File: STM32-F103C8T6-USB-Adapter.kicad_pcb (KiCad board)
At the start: 2 copper layers, 86 x 39 mm, 64 parts, among them J1 USB_B_Micro, J2 Conn_01x06_Male, J3 Conn_01x04_Male, J4 Conn_01x06_Male, J5 Conn_01x05_Male, J6 Conn_01x04_Male, J7 Conn_01x04_Male, Q1 BC817, SW1 SW_Push, U1 SN65220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

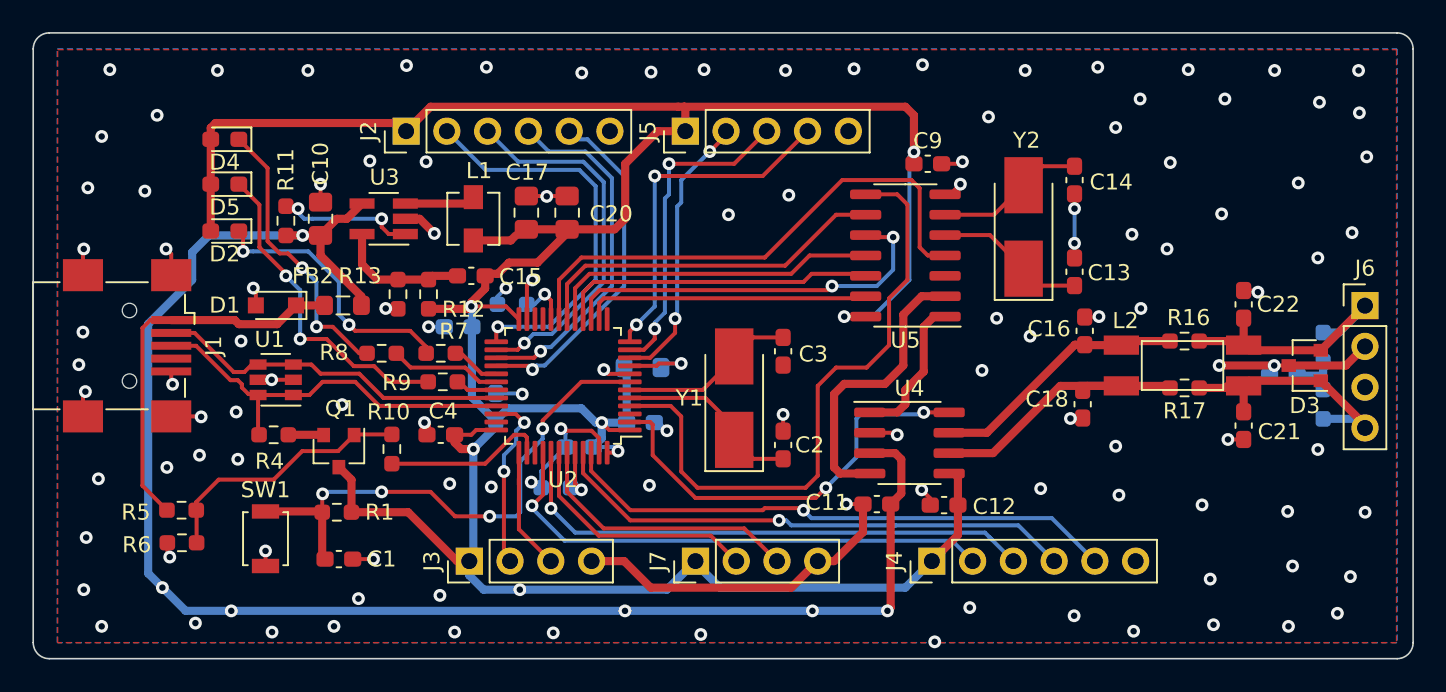
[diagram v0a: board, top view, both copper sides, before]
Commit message: optimize via of gnd copper
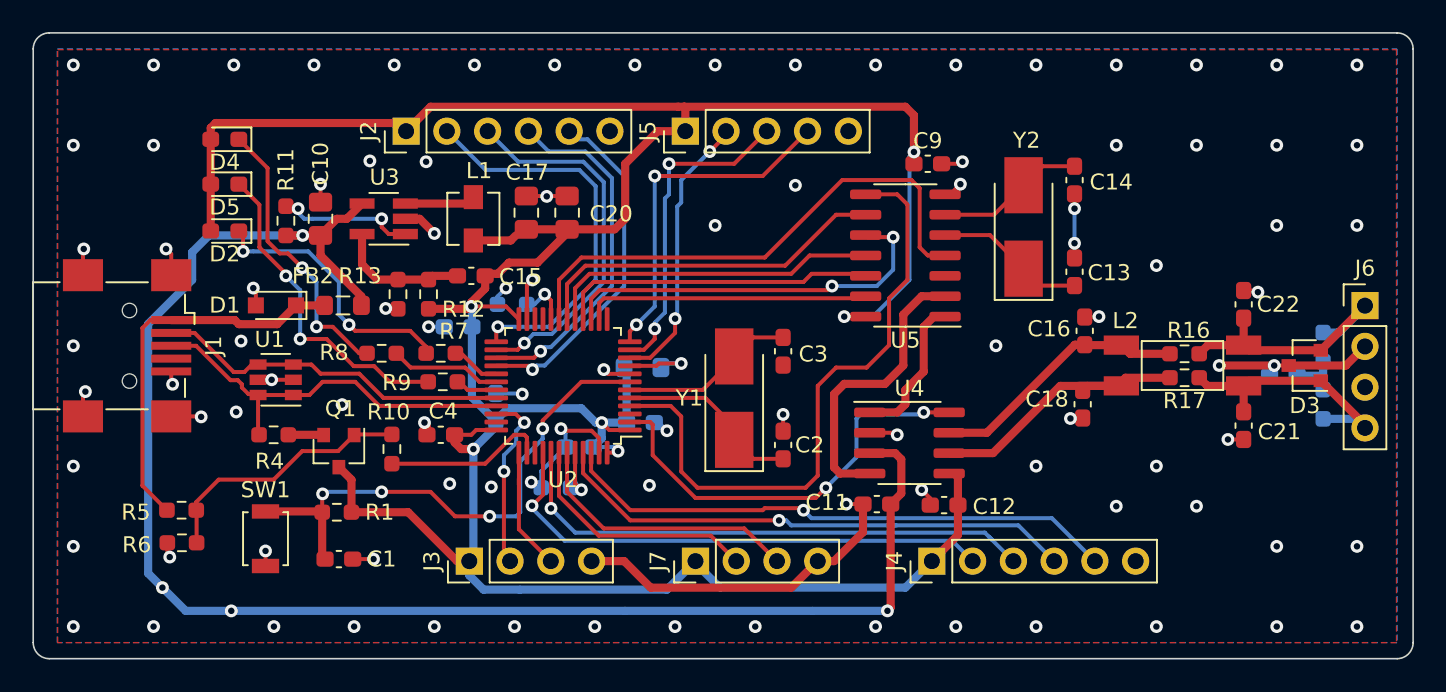
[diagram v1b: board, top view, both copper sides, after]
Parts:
- moved R16 0.79 mm to (171.8, 75.0)
- moved R17 0.63 mm to (171.8, 76.5)
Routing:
- net /CANL: track 18.3 -> 16.7 mm
- net GND: vias 118 -> 98
- net +5V: vias 6 -> 4
- net +3V3: vias 7 -> 6
- net (no net): vias 1 -> 0
